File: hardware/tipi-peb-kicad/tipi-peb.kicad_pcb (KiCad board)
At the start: 2 copper layers, 237.7 x 117.3 mm, 0 parts

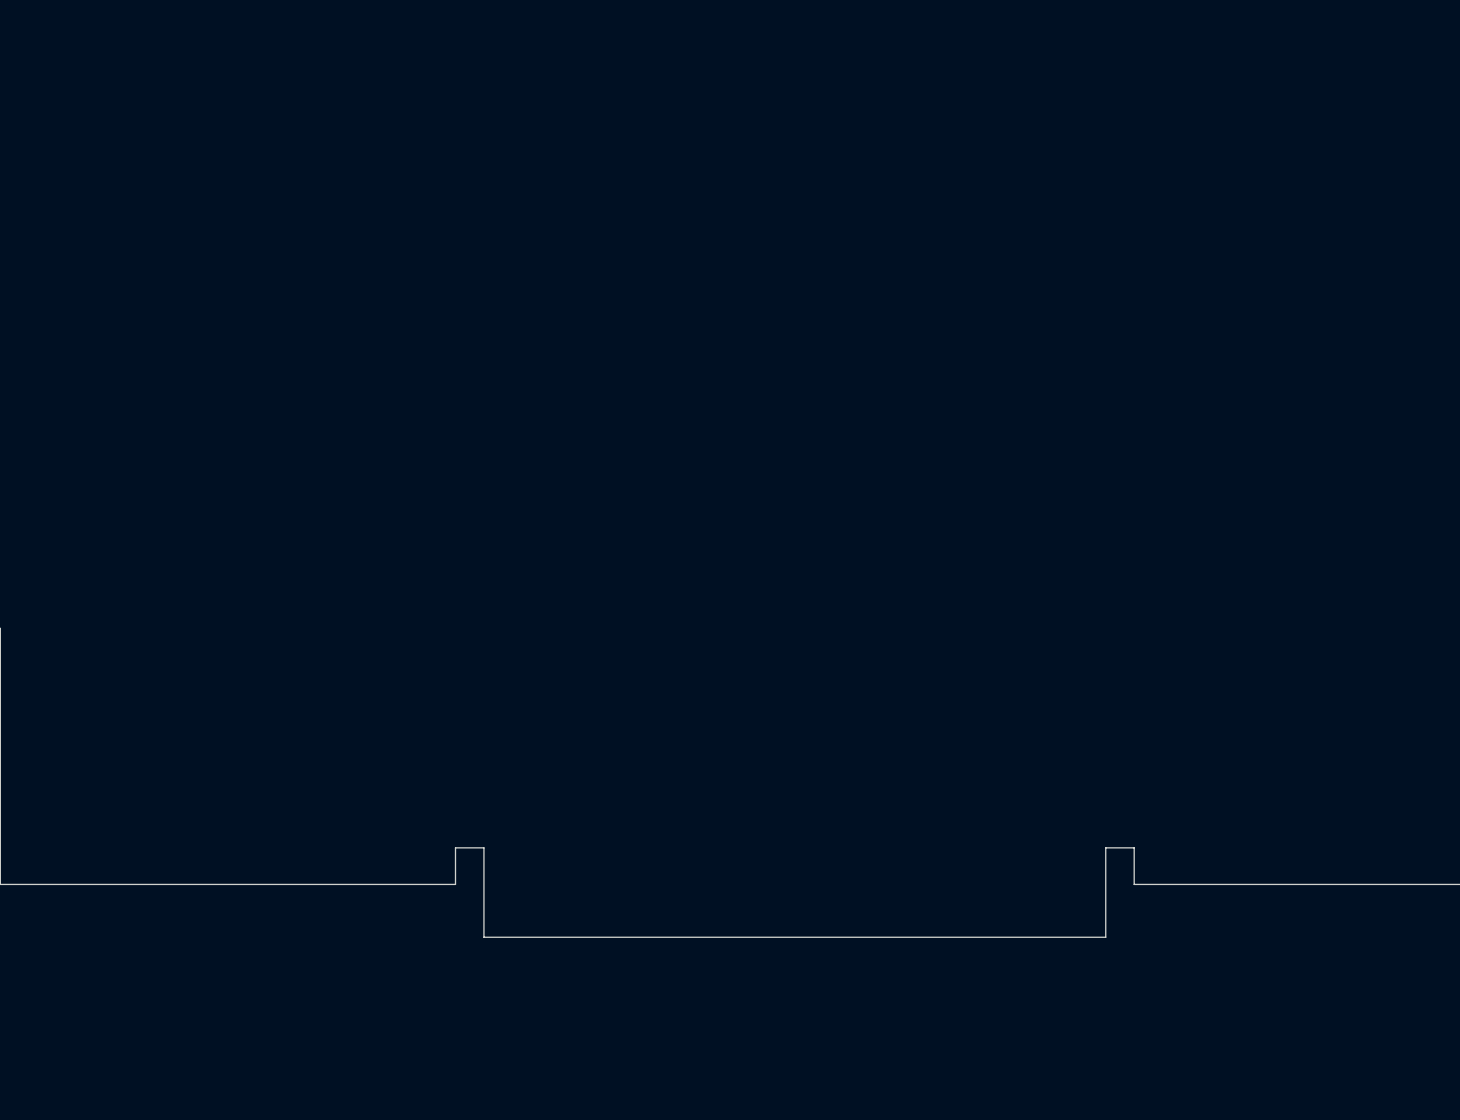
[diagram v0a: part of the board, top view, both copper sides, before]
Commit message: spread footprints out on peb pcboard.
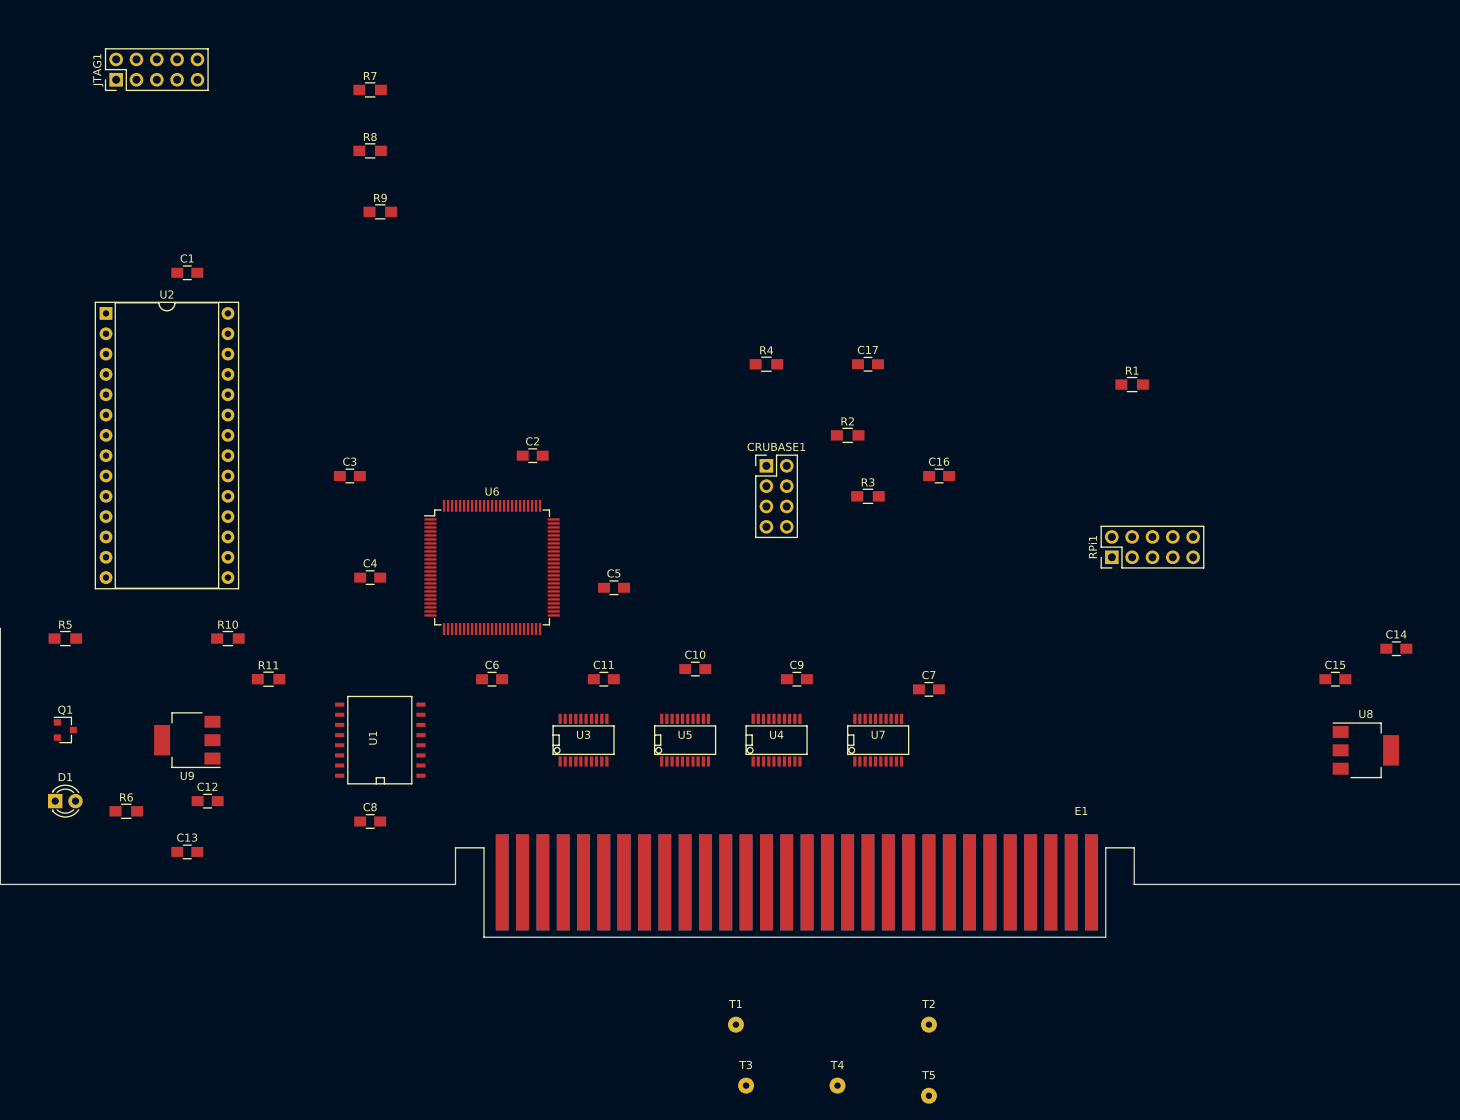
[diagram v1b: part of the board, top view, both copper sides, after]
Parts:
- added C1: 0.1uf, Capacitors_SMD:C_0805_HandSoldering, F.Cu at (127.0, 100.3)
- added C10: 0.1uf, Capacitors_SMD:C_0805_HandSoldering, F.Cu at (190.5, 149.9)
- added C11: 0.1uf, Capacitors_SMD:C_0805_HandSoldering, F.Cu at (179.1, 151.1)
- added C12: 0.1uf, Capacitors_SMD:C_0805_HandSoldering, F.Cu at (129.5, 166.4)
- added C13: 0.1uf, Capacitors_SMD:C_0805_HandSoldering, F.Cu at (127.0, 172.7)
- added C14: 10uf, Capacitors_SMD:C_0805_HandSoldering, F.Cu at (278.1, 147.3)
- added C15: 10uf, Capacitors_SMD:C_0805_HandSoldering, F.Cu at (270.5, 151.1)
- added C16: 22uf, Capacitors_SMD:C_0805_HandSoldering, F.Cu at (221.0, 125.7)
- added C17: 22uf, Capacitors_SMD:C_0805_HandSoldering, F.Cu at (212.1, 111.8)
- added C2: 0.1uf, Capacitors_SMD:C_0805_HandSoldering, F.Cu at (170.2, 123.2)
- added C3: 0.1uf, Capacitors_SMD:C_0805_HandSoldering, F.Cu at (147.3, 125.7)
- added C4: 0.1uf, Capacitors_SMD:C_0805_HandSoldering, F.Cu at (149.9, 138.4)
- added C5: 0.1uf, Capacitors_SMD:C_0805_HandSoldering, F.Cu at (180.3, 139.7)
- added C6: 0.1uf, Capacitors_SMD:C_0805_HandSoldering, F.Cu at (165.1, 151.1)
- added C7: 0.1uf, Capacitors_SMD:C_0805_HandSoldering, F.Cu at (219.7, 152.4)
- added C8: 0.1uf, Capacitors_SMD:C_0805_HandSoldering, F.Cu at (149.9, 168.9)
- added C9: 0.1uf, Capacitors_SMD:C_0805_HandSoldering, F.Cu at (203.2, 151.1)
- added CRUBASE1: CONN_02X04, Pin_Headers:Pin_Header_Straight_2x04_Pitch2.54mm, F.Cu at (199.4, 124.5)
- added D1: LED_ALT, LEDs:LED_D3.0mm, F.Cu at (110.5, 166.4)
- added E1: TiPEBEdge, peb-edge-card:ti99-peb-edge, F.Cu at (199.4, 176.5)
- added JTAG1: AVR-JTAG-10, Pin_Headers:Pin_Header_Straight_2x05_Pitch2.54mm, F.Cu at (118.1, 76.2)
- added Q1: Q_NPN_BCE, TO_SOT_Packages_SMD:SOT-23, F.Cu at (111.8, 157.5)
- added R1: 1k, Resistors_SMD:R_0805_HandSoldering, F.Cu at (245.1, 114.3)
- added R10: 4.7k, Resistors_SMD:R_0805_HandSoldering, F.Cu at (132.1, 146.1)
- added R11: 4.7k, Resistors_SMD:R_0805_HandSoldering, F.Cu at (137.2, 151.1)
- added R2: 1k, Resistors_SMD:R_0805_HandSoldering, F.Cu at (209.6, 120.7)
- added R3: 1k, Resistors_SMD:R_0805_HandSoldering, F.Cu at (212.1, 128.3)
- added R4: 1k, Resistors_SMD:R_0805_HandSoldering, F.Cu at (199.4, 111.8)
- added R5: 1k, Resistors_SMD:R_0805_HandSoldering, F.Cu at (111.8, 146.1)
- added R6: 330, Resistors_SMD:R_0805_HandSoldering, F.Cu at (119.4, 167.6)
- added R7: 10k, Resistors_SMD:R_0805_HandSoldering, F.Cu at (149.9, 77.5)
- added R8: 10k, Resistors_SMD:R_0805_HandSoldering, F.Cu at (149.9, 85.1)
- added R9: 10k, Resistors_SMD:R_0805_HandSoldering, F.Cu at (151.1, 92.7)
- added RPi1: RPI_CONN_02X05, Pin_Headers:Pin_Header_Straight_2x05_Pitch2.54mm, F.Cu at (242.6, 135.9)
- added T1: TEST_1P, Wire_Pads:SolderWirePad_single_0-8mmDrill, F.Cu at (195.6, 194.3)
- added T2: TEST_1P, Wire_Pads:SolderWirePad_single_0-8mmDrill, F.Cu at (219.7, 194.3)
- added T3: TEST_1P, Wire_Pads:SolderWirePad_single_0-8mmDrill, F.Cu at (196.8, 201.9)
- added T4: TEST_1P, Wire_Pads:SolderWirePad_single_0-8mmDrill, F.Cu at (208.3, 201.9)
- added T5: TEST_1P, Wire_Pads:SolderWirePad_single_0-8mmDrill, F.Cu at (219.7, 203.2)
- added U1: 74HCT138, SMD_Packages:SO-16-W, F.Cu at (151.1, 158.8)
- added U2: 27C256, Housings_DIP:DIP-28_W15.24mm_Socket, F.Cu at (116.8, 105.4)
- added U3: 74HCT244, SMD_Packages:SSOP-20, F.Cu at (176.5, 158.8)
- added U4: 74HCT244, SMD_Packages:SSOP-20, F.Cu at (200.7, 158.8)
- added U5: 74HCT244, SMD_Packages:SSOP-20, F.Cu at (189.2, 158.8)
- added U6: XC95144XL-TQ100, Housings_QFP:TQFP-100_14x14mm_Pitch0.5mm, F.Cu at (165.1, 137.2)
- added U7: 74HCT245, SMD_Packages:SSOP-20, F.Cu at (213.4, 158.8)
- added U8: LM1117-3.3, TO_SOT_Packages_SMD:SOT-223, F.Cu at (274.3, 160.0)
- added U9: LM7805_TO220, TO_SOT_Packages_SMD:SOT-223, F.Cu at (127.0, 158.8)

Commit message: a little layout progress
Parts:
- moved U9 162.0 mm to (288.9, 161.3), turned to 0 degrees
- moved T1 150.9 mm to (284.5, 72.4)
- moved T2 150.9 mm to (308.6, 72.4)
- moved T3 150.9 mm to (285.8, 80.0)
- moved T4 150.9 mm to (297.2, 80.0)
- moved T5 150.9 mm to (308.6, 81.3)
- moved C13 93.3 mm to (219.7, 162.6), turned to 270 degrees
- moved RPi1 91.4 mm to (323.9, 94.0), turned to 0 degrees
- moved R1 90.8 mm to (169.0, 163.8)
- moved U1 87.0 mm to (238.1, 157.5), turned to 0 degrees
- moved C17 84.3 mm to (279.4, 162.5), turned to 90 degrees
- moved U6 76.7 mm to (241.3, 128.2), turned to 180 degrees
- moved C16 63.2 mm to (281.9, 142.2), turned to 90 degrees
- moved C1 61.9 mm to (143.5, 160.0), turned to 180 degrees
- moved C2 57.3 mm to (114.3, 110.5), turned to 90 degrees
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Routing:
- net +8V: track 0.00 -> 63.5 mm, vias 0 -> 1
- net Net-(R1-Pad2): track 0.00 -> 23.9 mm, vias 0 -> 2
- net GND: track 0.00 -> 19.1 mm
- net TI_PH3: track 0.00 -> 15.5 mm, vias 0 -> 2
- net TI_CRUCLK: track 0.00 -> 13.5 mm, vias 0 -> 1
- net TI_A0: track 0.00 -> 13.3 mm, vias 0 -> 1
- net TI_A2: track 0.00 -> 13.2 mm, vias 0 -> 1
- net TI_DBIN: track 0.00 -> 13.0 mm
- net TI_WE: track 0.00 -> 13.0 mm
- net TI_A1: track 0.00 -> 12.7 mm
- net TI_A3: track 0.00 -> 12.7 mm
- net +5V: track 0.00 -> 6.48 mm
- net +3V3: track 0.00 -> 3.88 mm

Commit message: stash these changes.
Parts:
- moved R1 12.8 mm to (167.7, 151.1), turned to 180 degrees
- moved C8 10.9 mm to (188.0, 151.1), turned to 0 degrees
- moved C3 9.65 mm to (174.0, 151.1), turned to 0 degrees
- moved U4 6.48 mm to (202.0, 154.8)
- moved C13 6.48 mm to (221.0, 156.2)
- moved U7 6.48 mm to (215.0, 154.8)
- moved C4 6.48 mm to (196.8, 153.7)
- moved U3 3.64 mm to (174.1, 157.9), turned to 270 degrees
- moved U5 3.34 mm to (188.1, 157.9), turned to 270 degrees
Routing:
- net Net-(R1-Pad2): track 23.9 -> 0.00 mm, vias 2 -> 0
- net TI_PH3: track 15.5 -> 0.00 mm, vias 2 -> 0
- net TI_CRUCLK: track 13.5 -> 0.00 mm, vias 1 -> 0
- net TI_A0: track 13.3 -> 0.00 mm, vias 1 -> 0
- net TI_A2: track 13.2 -> 0.00 mm, vias 1 -> 0
- net TI_DBIN: track 13.0 -> 0.00 mm
- net TI_WE: track 13.0 -> 0.00 mm
- net TI_A3: track 12.7 -> 0.04 mm
- net TI_A1: track 12.7 -> 0.11 mm
- net GND: track 19.1 -> 14.7 mm

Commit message: about half routed
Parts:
- removed T1, T2, T3, T4, T5: TEST_1P, Wire_Pads:SolderWirePad_single_0-8mmDrill
- U1: footprint SMD_Packages:SO-16-W -> Housings_SSOP:TSSOP-16_4.4x5mm_Pitch0.65mm
- moved C5 151.8 mm to (262.1, 76.7), turned to 270 degrees
- moved C12 142.9 mm to (240.8, 76.7), turned to 270 degrees
- moved C6 139.9 mm to (251.0, 76.7), turned to 270 degrees
- moved U1 113.6 mm to (125.0, 147.6)
- moved JTAG1 113.5 mm to (227.6, 106.2)
- moved R7 95.2 mm to (237.7, 114.0), turned to 270 degrees
- moved R8 90.1 mm to (235.2, 114.0), turned to 270 degrees
- moved R9 84.2 mm to (232.7, 113.9), turned to 270 degrees
- moved C10 54.2 mm to (223.5, 76.7)
- moved C11 54.2 mm to (229.9, 76.7)
- moved C7 54.2 mm to (213.4, 76.7)
- moved C9 54.2 mm to (218.4, 76.7)
- moved C2 45.5 mm to (158.0, 123.2), turned to 0 degrees
- moved R3 37.4 mm to (183.1, 152.0), turned to 270 degrees
- moved R2 33.5 mm to (196.6, 151.6), turned to 270 degrees
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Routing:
- net GND: track 14.7 -> 101.0 mm, vias 0 -> 3
- net B_A10: track 0.00 -> 54.9 mm, vias 0 -> 2
- net B_A11: track 0.00 -> 53.2 mm, vias 0 -> 2
- net DB_EN: track 0.00 -> 52.8 mm, vias 0 -> 2
- net B_A4: track 0.00 -> 52.6 mm, vias 0 -> 2
- net B_A5: track 0.00 -> 52.4 mm, vias 0 -> 2
- net B_A3: track 0.00 -> 49.4 mm, vias 0 -> 2
- net B_A7: track 0.00 -> 48.9 mm, vias 0 -> 2
- net B_A6: track 0.00 -> 48.2 mm, vias 0 -> 2
- net B_A8: track 0.00 -> 45.1 mm, vias 0 -> 2
- net B_A2: track 0.00 -> 44.1 mm, vias 0 -> 2
- net B_A12: track 0.00 -> 42.3 mm
- net B_A14: track 0.00 -> 42.0 mm
- net B_A13: track 0.00 -> 42.0 mm
- net B_A9: track 0.00 -> 41.7 mm, vias 0 -> 2
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
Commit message: 2/3rds routed
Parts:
- moved C5 58.7 mm to (223.8, 121.1), turned to 90 degrees
- moved R10 48.7 mm to (155.5, 169.7), turned to 0 degrees
- moved R11 48.2 mm to (155.5, 166.6), turned to 0 degrees
- moved C1 31.0 mm to (138.2, 170.9)
- moved U1 30.2 mm to (146.4, 168.8), turned to 180 degrees
- moved R5 10.6 mm to (117.3, 158.2), turned to 180 degrees
- moved R1 9.23 mm to (168.7, 152.7)
- moved RPi1 1.83 mm to (322.3, 93.0)
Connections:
- E1 pad 56: TI_AMD -> TI_MEMEN
- R10 pad 2: +5V -> Net-(R10-Pad2)
- R11 pad 2: GND -> Net-(R11-Pad2)
- U1 pad 4: TI_AMD -> TI_MEMEN
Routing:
- net LED0: track 0.00 -> 147.8 mm, vias 0 -> 2
- net GND: track 101.0 -> 218.3 mm, vias 3 -> 29
- net TI_AMD: track 0.00 -> 98.9 mm, vias 0 -> 2
- net TI_CRUIN: track 0.00 -> 81.2 mm, vias 0 -> 3
- net B_MEMEN: track 0.00 -> 79.8 mm, vias 0 -> 2
- net DSR_EN: track 0.00 -> 72.3 mm, vias 0 -> 2
- net RDBENA: track 0.00 -> 69.8 mm, vias 0 -> 1
- net B_PH3: track 0.00 -> 68.6 mm, vias 0 -> 2
- net TP_D2: track 32.4 -> 99.5 mm, vias 2 -> 3
- net TP_D0: track 34.4 -> 100.9 mm, vias 0 -> 1
- net DSR_B0: track 0.00 -> 65.9 mm, vias 0 -> 1
- net TP_D1: track 33.6 -> 98.8 mm, vias 0 -> 1
- net DSR_B1: track 0.00 -> 63.7 mm, vias 0 -> 1
- net B_A11: track 53.2 -> 115.2 mm
- net B_DBIN: track 0.00 -> 60.3 mm, vias 0 -> 2
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- added copper zone on B.Cu, net GND

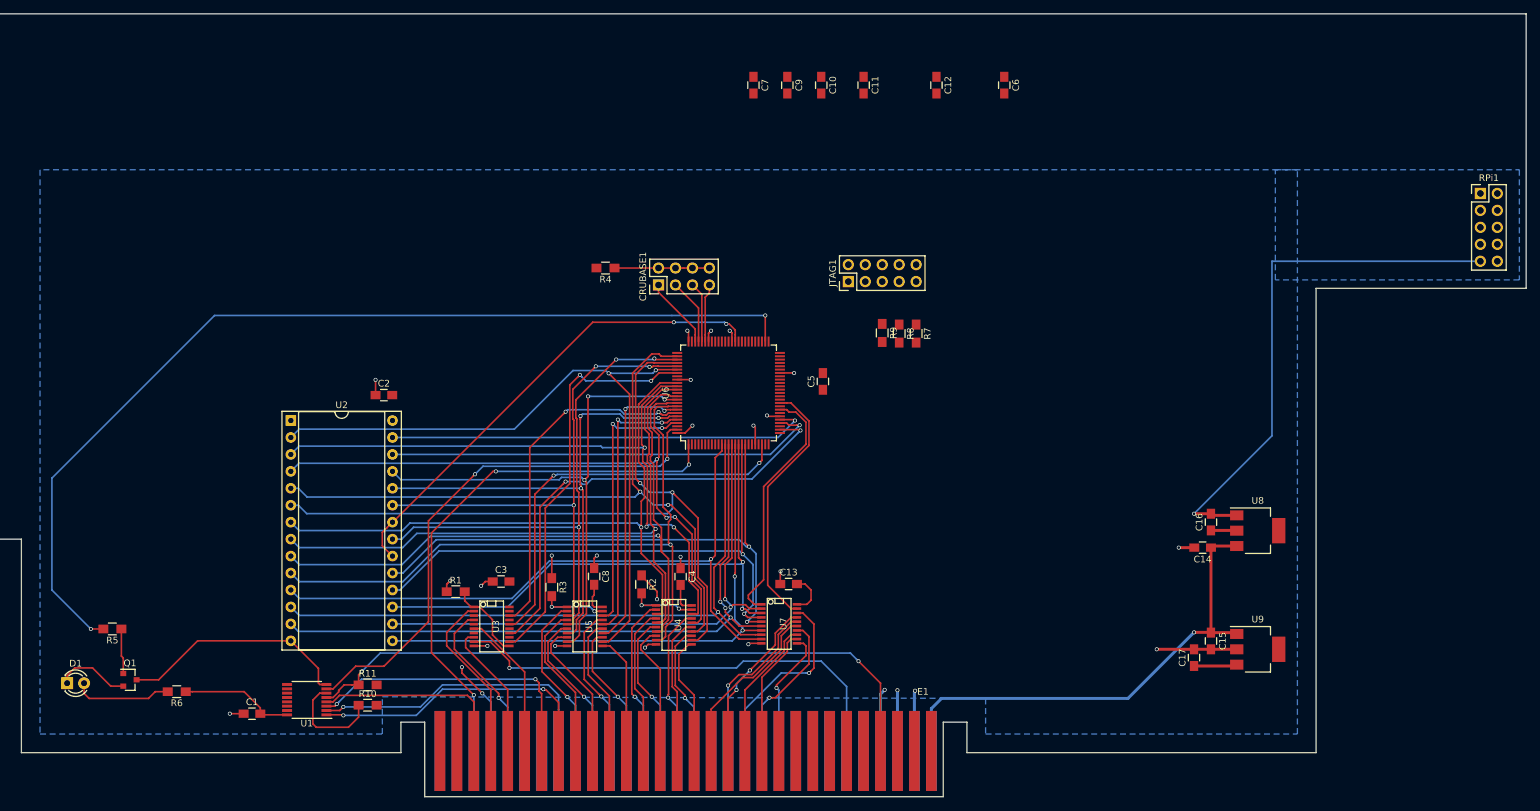
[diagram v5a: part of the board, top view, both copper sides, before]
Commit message: data lines wired, room for PI mounting
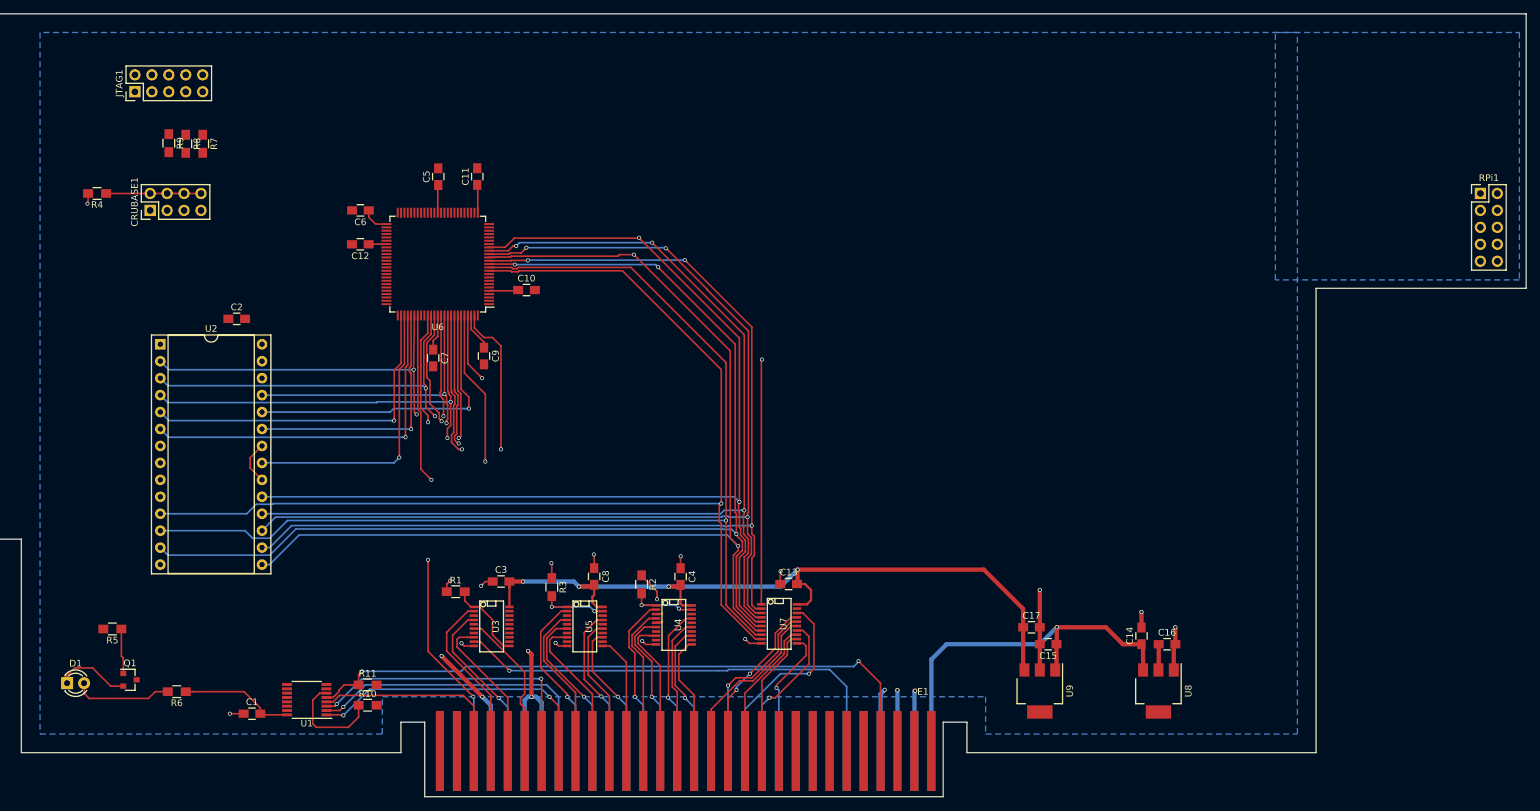
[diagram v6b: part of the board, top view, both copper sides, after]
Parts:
- moved JTAG1 110.7 mm to (120.7, 77.7)
- moved R7 110.7 mm to (130.8, 85.5)
- moved R8 110.7 mm to (128.3, 85.5)
- moved R9 110.7 mm to (125.7, 85.4)
- moved C6 98.3 mm to (154.5, 95.5), turned to 180 degrees
- moved C12 89.6 mm to (154.4, 100.6), turned to 180 degrees
- moved CRUBASE1 77.0 mm to (122.9, 95.5)
- moved R4 77.0 mm to (115.0, 93.0)
- moved C5 65.3 mm to (166.1, 90.4)
- moved C7 63.1 mm to (165.4, 117.6)
- moved C9 61.0 mm to (173.0, 117.3)
- moved C11 59.5 mm to (172.0, 90.4), turned to 90 degrees
- moved C10 53.8 mm to (179.3, 107.4), turned to 0 degrees
- moved U6 47.7 mm to (166.0, 103.6), turned to 180 degrees
- moved U9 33.3 mm to (256.3, 167.5), turned to 270 degrees
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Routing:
- net LED0: track 147.8 -> 0.00 mm, vias 2 -> 0
- net +5V: track 40.2 -> 133.8 mm, vias 0 -> 4
- net GND: track 218.3 -> 125.2 mm, vias 29 -> 23
- net B_A14: track 101.7 -> 15.4 mm
- net TP_D4: track 82.1 -> 162.1 mm, vias 2 -> 3
- net B_A15: track 100.9 -> 21.5 mm
- net B_A13: track 98.4 -> 19.2 mm
- net TP_D5: track 83.4 -> 162.4 mm, vias 2 -> 3
- net B_A12: track 96.1 -> 18.8 mm
- net TP_D6: track 84.6 -> 161.5 mm, vias 2 -> 3
- net TP_D3: track 84.3 -> 161.1 mm
- net TP_D2: track 99.5 -> 175.7 mm
- net TP_D7: track 86.0 -> 161.4 mm
- net TP_D1: track 98.8 -> 171.4 mm
- net B_PH3: track 68.6 -> 0.00 mm, vias 2 -> 0
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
